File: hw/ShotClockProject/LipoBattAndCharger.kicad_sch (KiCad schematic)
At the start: 17 parts, among them IC1 TP4056-42-ESOP8, J2 Conn_01x02_Pin, J8 Conn_01x03_Pin, J9 Conn_01x03_Pin, Q1 Q_PMOS_SGD

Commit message: HW change for testing
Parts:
- added J10: Conn_01x03_Pin, symbol Connector:Conn_01x03_Pin
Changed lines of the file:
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@@
+    )
+  )
+  (symbol (lib_id "Connector:Conn_01x03_Pin") (at 73.66 124.46 0) (unit 1)
+    (in_bom yes) (on_board yes) (dnp no)
+    (property "Reference" "J10" (at 72.39 115.57 0)
+      (effects (font (size 1.27 1.27)))
+    )
+    (property "Value" "Conn_01x03_Pin" (at 72.39 118.11 0)
+      (effects (font (size 1.27 1.27)))
+    )
+    (property "Footprint" "" (at 73.66 124.46 0)
+      (effects (font (size 1.27 1.27)) hide)
+    )
+    (property "Datasheet" "~" (at 73.66 124.46 0)
+      (effects (font (size 1.27 1.27)) hide)
+    )
+    (pin "1")
+    (pin "2")
+    (pin "3")
+    (instances
+      (project "ShotClockProject"
+        (path "/5fd859aa-754d-49c2-9762-3f7ebe3bb64c/d287d155-1951-4d4f-8d6c-570f03bc79f5"
+          (reference "J10") (unit 1)
+        )
+      )
     )
   )

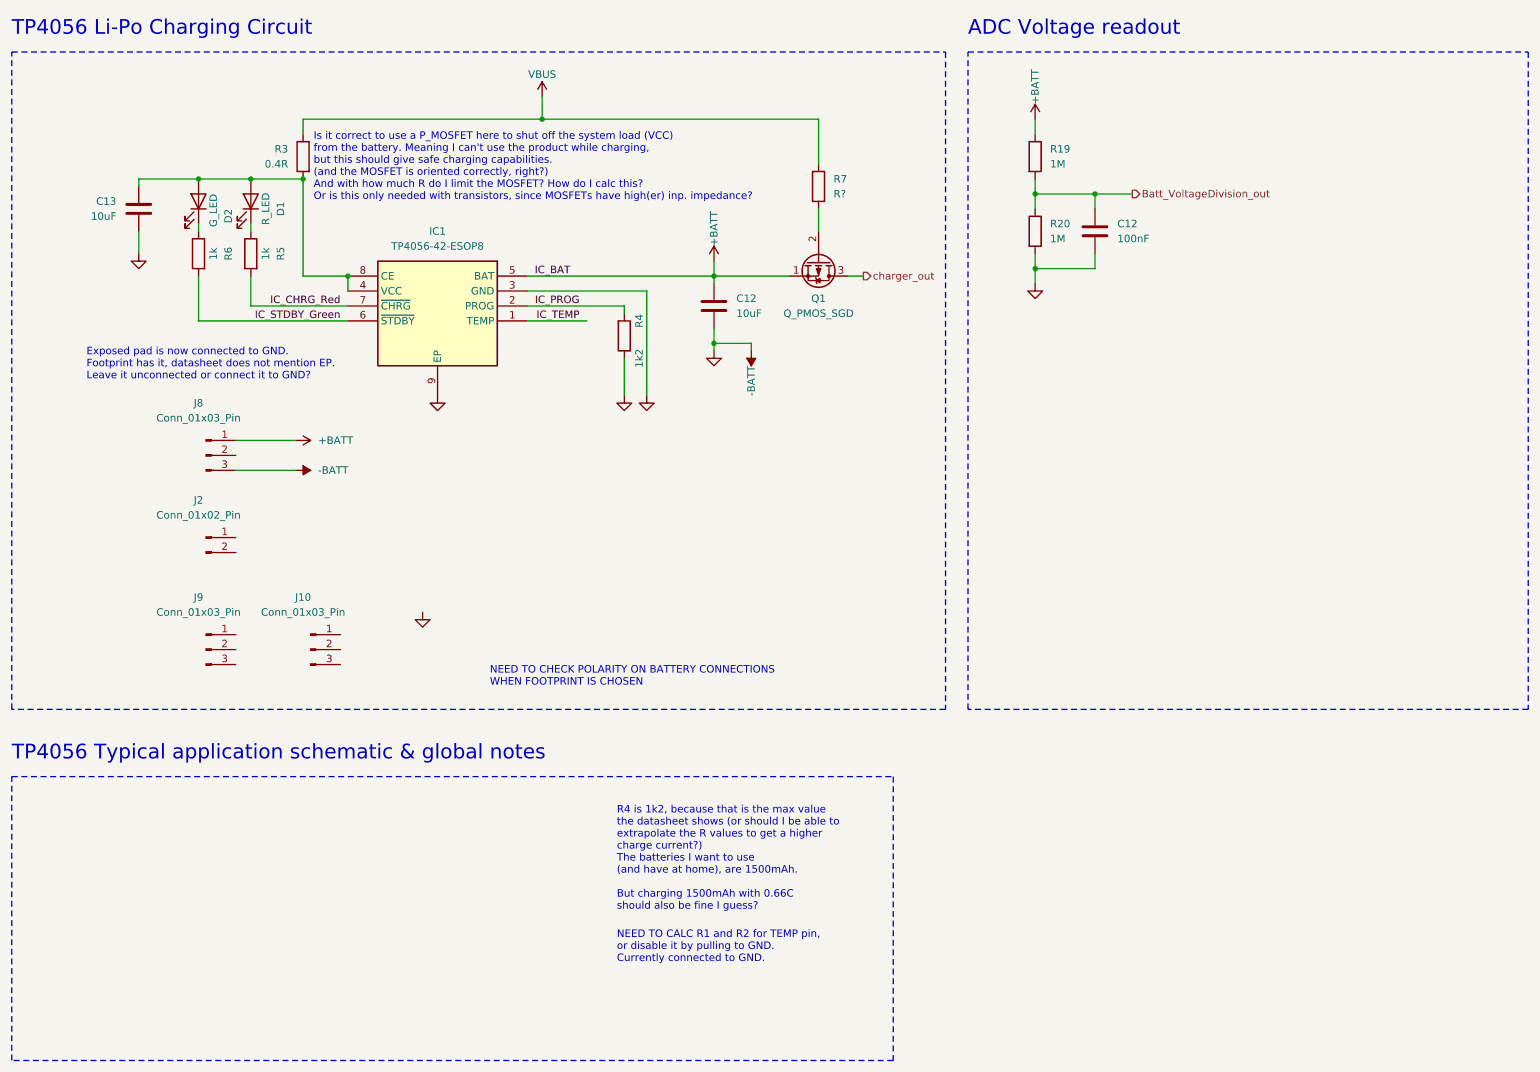
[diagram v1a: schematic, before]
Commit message: Changed documentation, added to schematics
Added Vbat connection via LDO
Added jumper to enable/disable the TEMP pin of chrg IC.
Added PDF exports of schematics
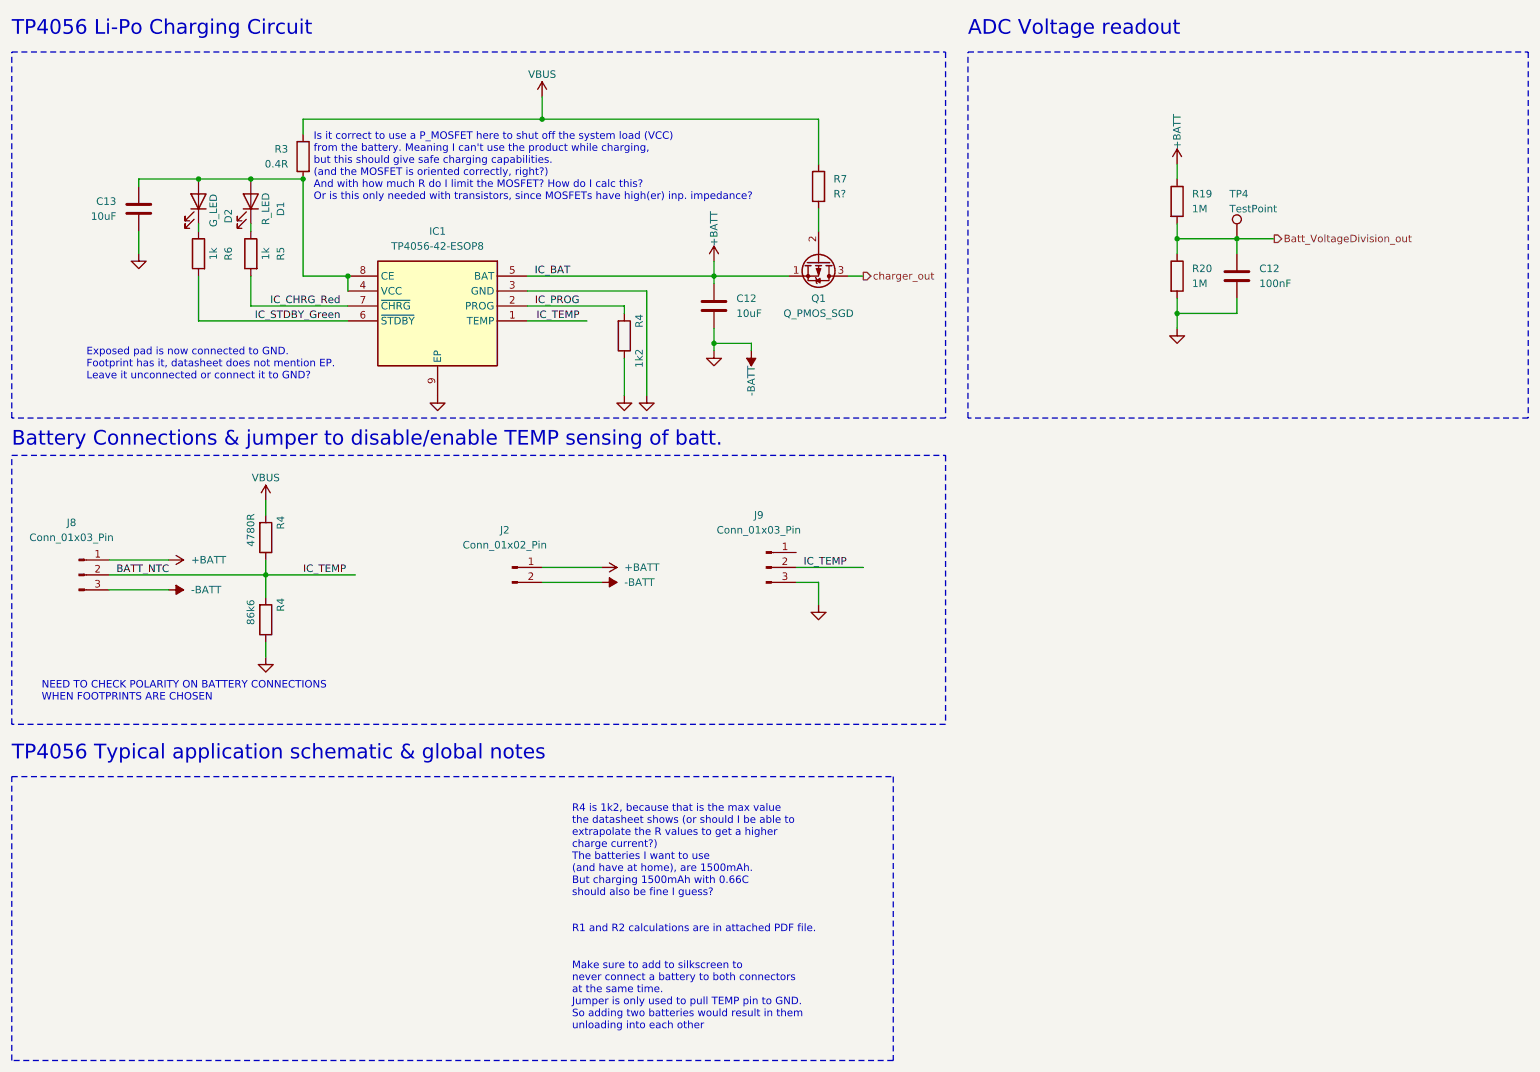
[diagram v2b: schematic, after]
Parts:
- removed J10: Conn_01x03_Pin, symbol Connector:Conn_01x03_Pin
- added R4: 86k6, symbol Device:R
- added R4: 4780R, symbol Device:R
- added TP4: TestPoint, symbol Connector:TestPoint
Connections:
- net IC_TEMP is gone; now on net BATT_NTC: IC1.1 (TEMP)
- net +BATT: now also J2.1 (Pin_1)
- net -BATT: now also J2.2 (Pin_2), J9.3 (Pin_3), R4.1
- net Batt_VoltageDivision_out: now also TP4.1
- net VBUS: now also R4.2
- net BATT_NTC: now reaches J9.2 (Pin_2)
- net BATT_NTC: now also J8.2 (Pin_2), R4.1, R4.2
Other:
- note added: "Battery Connections & jumper to disable/enable TEMP sensing of batt."
- note added: "Make sure to add to silkscreen to never connect a battery to both connectors at the same time. Jumper is only used to pull TEMP pin to GND. So adding two batteries would result in them unloading into each other"
- note added: "NEED TO CHECK POLARITY ON BATTERY CONNECTIONS WHEN FOOTPRINTS ARE CHOSEN"
- note added: "R4 is 1k2, because that is the max value the datasheet shows (or should I be able to extrapolate the R values to get a higher charge current?) The batteries I want to use (and have at home), are 1500mAh. But charging 1500mAh with 0.66C should also be fine I guess? R1 and R2 calculations are in attached PDF file."
- note removed: "NEED TO CALC R1 and R2 for TEMP pin, or disable it by pulling to GND. Currently connected to GND."
- note removed: "NEED TO CHECK POLARITY ON BATTERY CONNECTIONS WHEN FOOTPRINT IS CHOSEN"
- note removed: "R4 is 1k2, because that is the max value the datasheet shows (or should I be able to extrapolate the R values to get a higher charge current?) The batteries I want to use (and have at home), are 1500mAh. But charging 1500mAh with 0.66C should also be fine I guess?"
- moved on the sheet: C12, J2, J8, J9, R19, R20

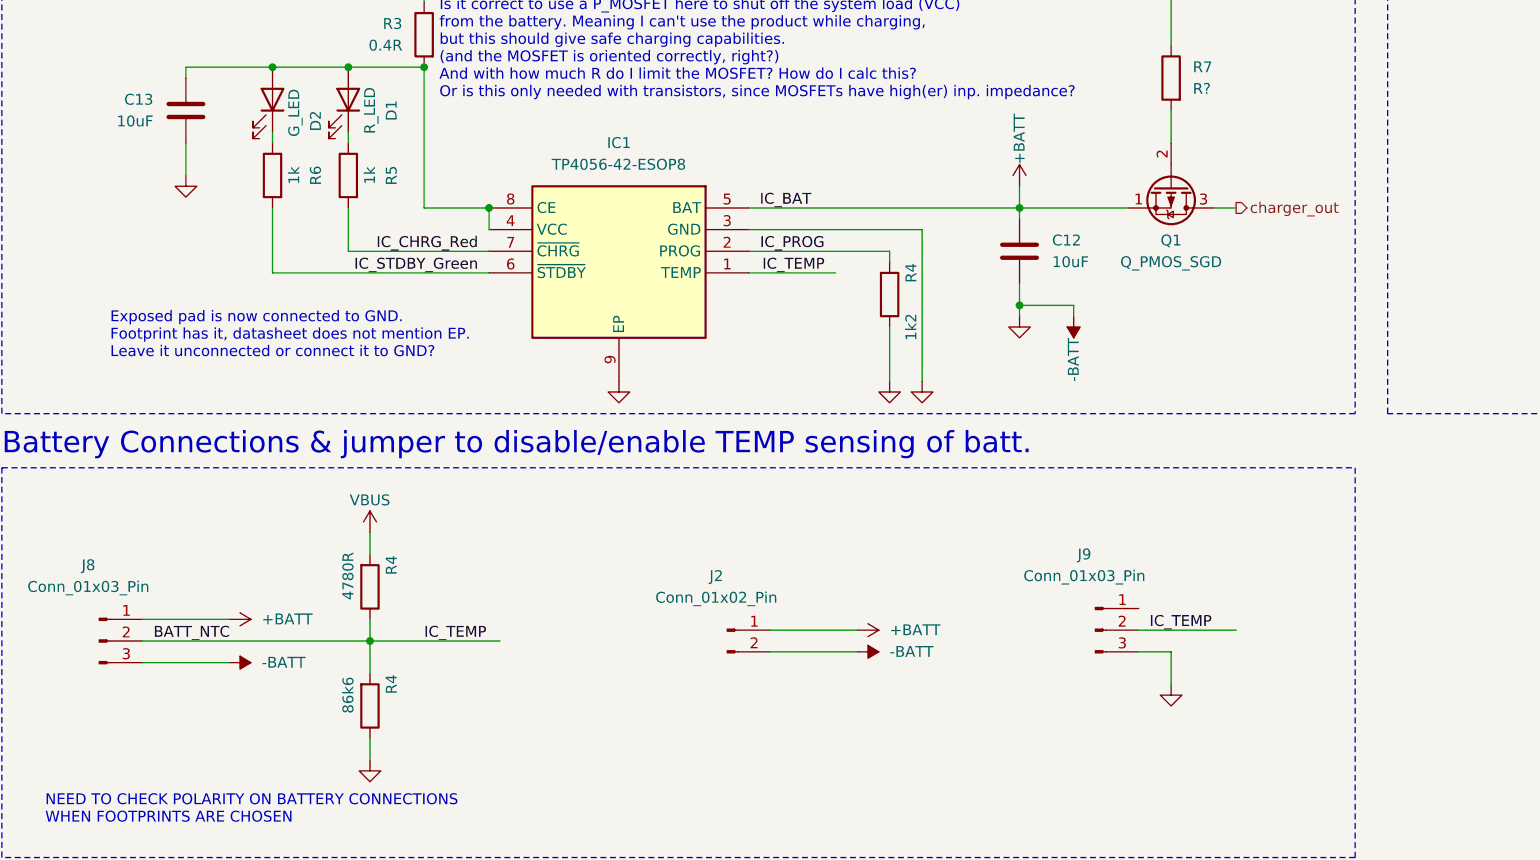
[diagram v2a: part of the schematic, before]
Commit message: Fixed all ERC issues
Mainly by placing PWR_FLAGs and NetTies to show KiCAD where the GNDs are connected to each other physically, without them being the same net.
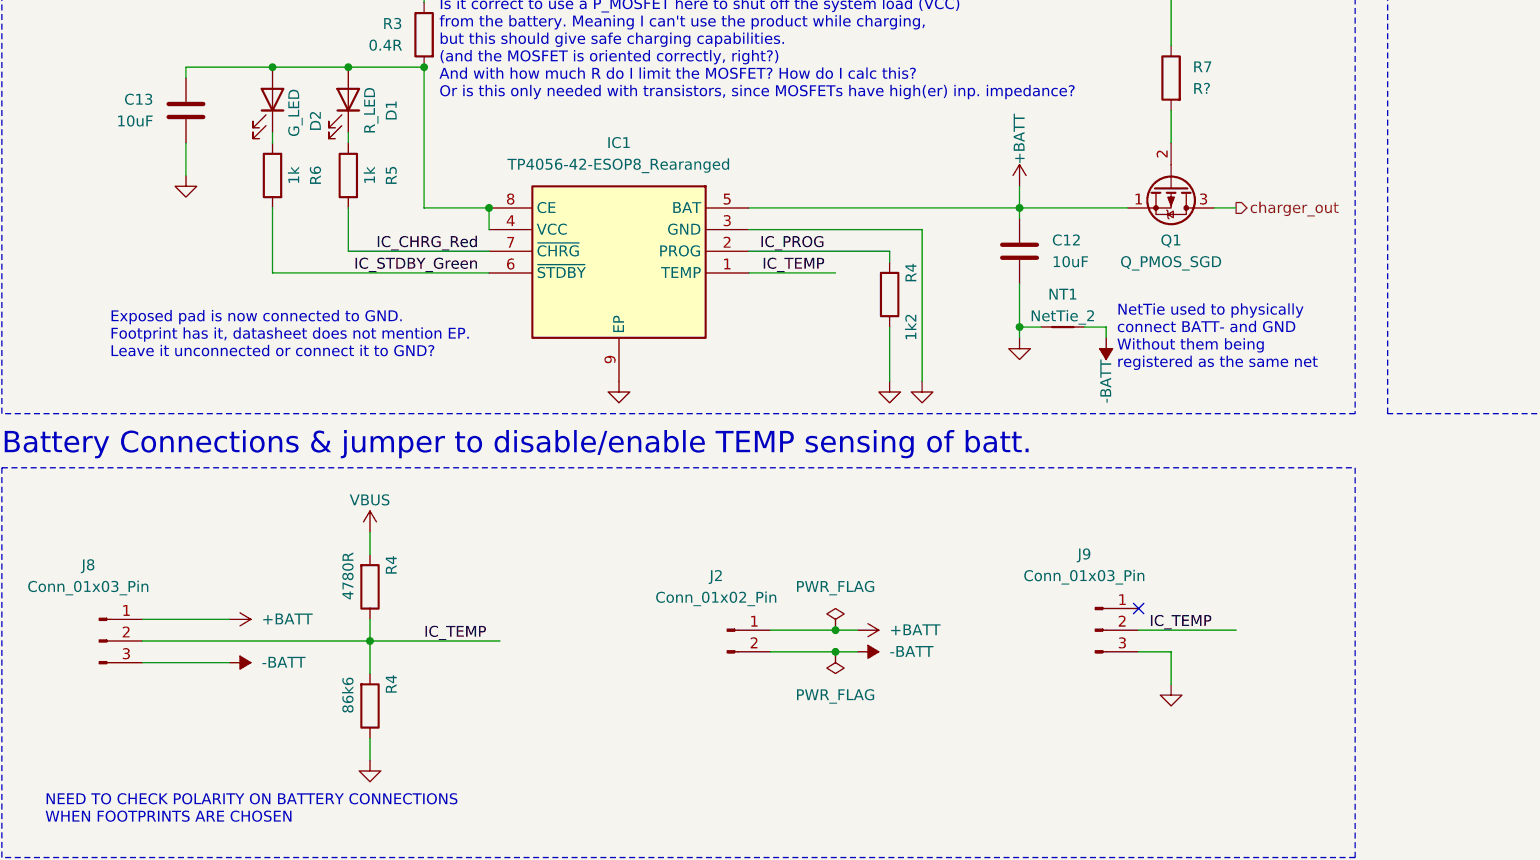
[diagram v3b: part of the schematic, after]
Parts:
- added NT1: NetTie_2, symbol Device:NetTie_2
- IC1: value TP4056-42-ESOP8 -> TP4056-42-ESOP8_Rearanged; symbol TP4056-42-ESOP8:TP4056-42-ESOP8 -> TP4056-42-ESOP8:TP4056-42-ESOP8_Rearanged
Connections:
- net -BATT: now also NT1.2; no longer C12.2, C12.2, C13.2, IC1.3 (GND), IC1.9 (EP), J9.3 (Pin_3), R20.2, R4.1, R4.1
- net BATT_NTC renamed IC_TEMP
- new net GND: C12.2, C12.2, C13.2, IC1.3 (GND), IC1.9 (EP), J9.3 (Pin_3), NT1.1, R20.2, R4.1, R4.1
- no-connect marks 0 -> 1
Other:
- note added: "NetTie used to physically connect BATT- and GND Without them being registered as the same net"

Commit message: Init of SW, changes on HW
SW init STMIDE project
HW Added first few footprints for passive components.
Removed old name .IOC file
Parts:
- C12, C13: footprint (none) -> Capacitor_SMD:C_0402_1005Metric
- D1, D2: footprint (none) -> LED_SMD:LED_0603_1608Metric
- IC1: footprint SOIC127P600X175-9N -> Package_SO:Texas_HSOP-8-1EP_3.9x4.9mm_P1.27mm_ThermalVias
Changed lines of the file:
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@@
       (effects (font (size 1.27 1.27)) (justify right))
     )
-    (property "Footprint" "" (at 54.61 48.26 0)
+    (property "Footprint" "LED_SMD:LED_0603_1608Metric" (at 54.61 48.26 0)
       (effects (font (size 1.27 1.27)) hide)
     )
@@
       (effects (font (size 1.27 1.27)) (justify left))
     )
-    (property "Footprint" "" (at 143.2052 69.85 0)
+    (property "Footprint" "Capacitor_SMD:C_0402_1005Metric" (at 143.2052 69.85 0)
       (effects (font (size 1.27 1.27)) hide)
     )
@@
       (effects (font (size 1.27 1.27)))
     )
-    (property "Footprint" "" (at 63.5 48.26 0)
+    (property "Footprint" "LED_SMD:LED_0603_1608Metric" (at 63.5 48.26 0)
       (effects (font (size 1.27 1.27)) hide)
     )
@@
       (effects (font (size 1.27 1.27)))
     )
-    (property "Footprint" "SOIC127P600X175-9N" (at 83.82 155.88 0)
+    (property "Footprint" "Package_SO:Texas_HSOP-8-1EP_3.9x4.9mm_P1.27mm_ThermalVias" (at 83.82 155.88 0)
       (effects (font (size 1.27 1.27)) (justify left top) hide)
     )
@@
       (effects (font (size 1.27 1.27)) (justify left))
     )
-    (property "Footprint" "" (at 43.4848 53.34 0)
+    (property "Footprint" "Capacitor_SMD:C_0402_1005Metric" (at 43.4848 53.34 0)
       (effects (font (size 1.27 1.27)) hide)
     )
@@
       (effects (font (size 1.27 1.27)) (justify left))
     )
-    (property "Footprint" "" (at 232.1052 64.77 0)
-      (effects (font (size 1.27 1.27)) hide)
-    )
+    (property "Footprint" "Capacitor_SMD:C_0402_1005Metric" (at 232.1052 64.77 0)
+      (effects (font (size 1.27 1.27)) hide)
+    )
